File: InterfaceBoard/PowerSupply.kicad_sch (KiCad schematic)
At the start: 15 parts, among them U5 AP62250Z6

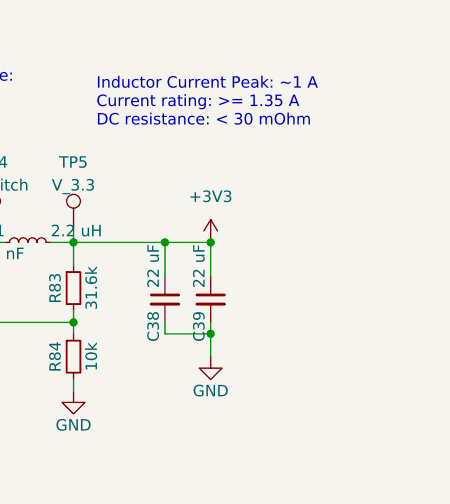
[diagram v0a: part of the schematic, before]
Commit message: InterfaceBoard: Routed some digital interfaces to MCU
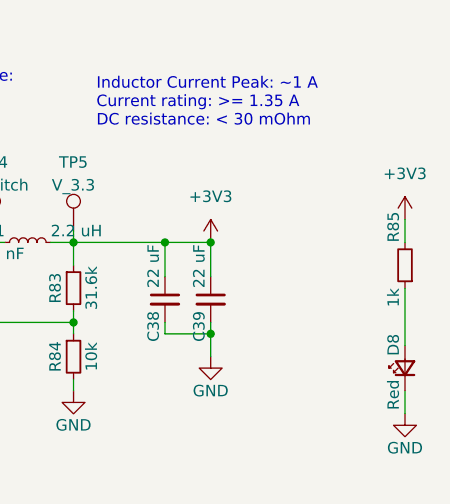
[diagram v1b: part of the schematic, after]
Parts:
- added D8: Red, LED_SMD:LED_0603_1608Metric, symbol Device:LED_Small
- added R85: 1k, Resistor_SMD:R_0603_1608Metric, symbol Device:R_Small
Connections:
- net +3V3: now also R85.2
- net GND: now also D8.1 (K)
- new net: D8.2 (A), R85.1
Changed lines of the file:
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@@
+    (stroke (width 0) (type default) (color 0 0 0 0))
+  )
+  (wire (pts (xy 213.36 87.63) (xy 213.36 90.17))
     (stroke (width 0) (type default) (color 0 0 0 0))
   )
@@
     (stroke (width 0) (type default) (color 0 0 0 0))
   )
+  (wire (pts (xy 213.36 106.68) (xy 213.36 109.22))
+    (stroke (width 0) (type default) (color 0 0 0 0))
+  )
   (wire (pts (xy 166.37 95.25) (xy 166.37 99.06))
     (stroke (width 0) (type default) (color 0 0 0 0))
@@
   )
   (wire (pts (xy 129.54 101.6) (xy 129.54 100.33))
+    (stroke (width 0) (type default) (color 0 0 0 0))
+  )
+  (wire (pts (xy 213.36 95.25) (xy 213.36 101.6))
     (stroke (width 0) (type default) (color 0 0 0 0))
   )
@@
     (effects (font (size 1.27 1.27)) (justify right))
   )
+  (symbol (lib_id "Device:R_Small") (at 213.36 92.71 180) (unit 1)
+    (in_bom yes) (on_board yes)
+    (property "Reference" "R85" (id 0) (at 212.09 90.17 90)
+      (effects (font (size 1.27 1.27)) (justify right))
+    )
+    (property "Value" "1k" (id 1) (at 212.09 95.25 90)
+      (effects (font (size 1.27 1.27)) (justify left))
+    )
+    (property "Footprint" "Resistor_SMD:R_0603_1608Metric" (id 2) (at 213.36 92.71 0)
+      (effects (font (size 1.27 1.27)) hide)
+    )
+    (property "Datasheet" "~" (id 3) (at 213.36 92.71 0)
+      (effects (font (size 1.27 1.27)) hide)
+    )
+    (pin "1")
+    (pin "2")
+  )
   (symbol (lib_id "power:GND") (at 176.53 106.68 0) (unit 1)
     (in_bom yes) (on_board yes)
@@
     )
     (pin "1")
+  )
+  (symbol (lib_id "Device:LED_Small") (at 213.36 104.14 90) (unit 1)
+    (in_bom yes) (on_board yes)
+    (property "Reference" "D8" (id 0) (at 212.09 100.33 0)
+      (effects (font (size 1.27 1.27)) (justify right))
+    )
+    (property "Value" "Red" (id 1) (at 212.09 105.41 0)
+      (effects (font (size 1.27 1.27)) (justify right))
+    )
+    (property "Footprint" "LED_SMD:LED_0603_1608Metric" (id 2) (at 213.36 104.14 90)
+      (effects (font (size 1.27 1.27)) hide)
+    )
+    (property "Datasheet" "~" (id 3) (at 213.36 104.14 90)
+      (effects (font (size 1.27 1.27)) hide)
+    )
+    (pin "1")
+    (pin "2")
   )
   (symbol (lib_id "power:GND") (at 148.59 101.6 0) (unit 1)
@@
     (pin "1")
   )
+  (symbol (lib_id "power:GND") (at 213.36 109.22 0) (unit 1)
+    (in_bom yes) (on_board yes)
+    (property "Reference" "#PWR0186" (id 0) (at 213.36 115.57 0)
+      (effects (font (size 1.27 1.27)) hide)
+    )
+    (property "Value" "GND" (id 1) (at 213.36 113.03 0))
+    (property "Footprint" "" (id 2) (at 213.36 109.22 0)
+      (effects (font (size 1.27 1.27)) hide)
+    )
+    (property "Datasheet" "" (id 3) (at 213.36 109.22 0)
+      (effects (font (size 1.27 1.27)) hide)
+    )
+    (pin "1")
+  )
   (symbol (lib_id "power:+3V3") (at 191.77 90.17 0) (unit 1)
     (in_bom yes) (on_board yes) (fields_autoplaced)
@@
     (pin "2")
   )
+  (symbol (lib_id "power:+3V3") (at 213.36 87.63 0) (unit 1)
+    (in_bom yes) (on_board yes) (fields_autoplaced)
+    (property "Reference" "#PWR0185" (id 0) (at 213.36 91.44 0)
+      (effects (font (size 1.27 1.27)) hide)
+    )
+    (property "Value" "+3V3" (id 1) (at 213.36 82.55 0))
+    (property "Footprint" "" (id 2) (at 213.36 87.63 0)
+      (effects (font (size 1.27 1.27)) hide)
+    )
+    (property "Datasheet" "" (id 3) (at 213.36 87.63 0)
+      (effects (font (size 1.27 1.27)) hide)
+    )
+    (pin "1")
+  )
   (symbol (lib_id "Device:C_Small") (at 163.83 92.71 90) (unit 1)

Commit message: InterfaceBoard: Rev 1.0
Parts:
- removed R80, R81, R82: 0, Resistor_SMD:R_0603_1608Metric, symbol Device:R_Small
- added J5: Conn_02x03_Odd_Even, Connector_PinHeader_1.27mm:PinHeader_2x03_P1.27mm_Vertical, symbol Connector_Generic:Conn_02x03_Odd_Even
- TP4: renamed from TP5; value V_3.3 -> 3V3
- renumbered C37 to C12, C35 to C13, C36 to C14, C39 to C15, C38 to C16, D8 to D3, R85 to R24, R84 to R29, R83 to R32, TP4 to TP7, U5 to U3
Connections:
- net +15V: now also J5.3 (Pin_3)
- net V_EXT: now also J5.5 (Pin_5)
- net V_IN: now also J5.2 (Pin_2), J5.4 (Pin_4), J5.6 (Pin_6)
- net V_USB: now also J5.1 (Pin_1)
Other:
- note removed: "Only populate one Or use diodes"
- company: (none) -> Peter Farley
- title: (none) -> Kiethley 615 Interface Board

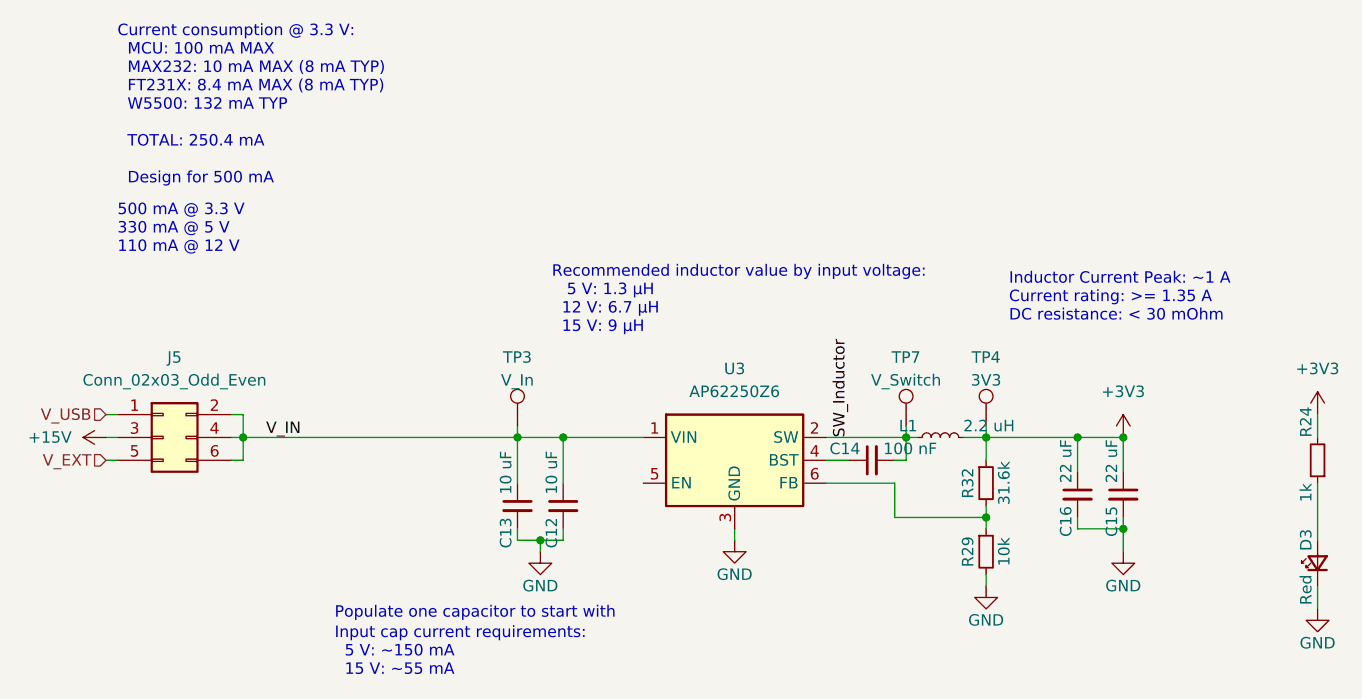
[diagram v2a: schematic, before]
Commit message: InterfaceBoard: Add BOM
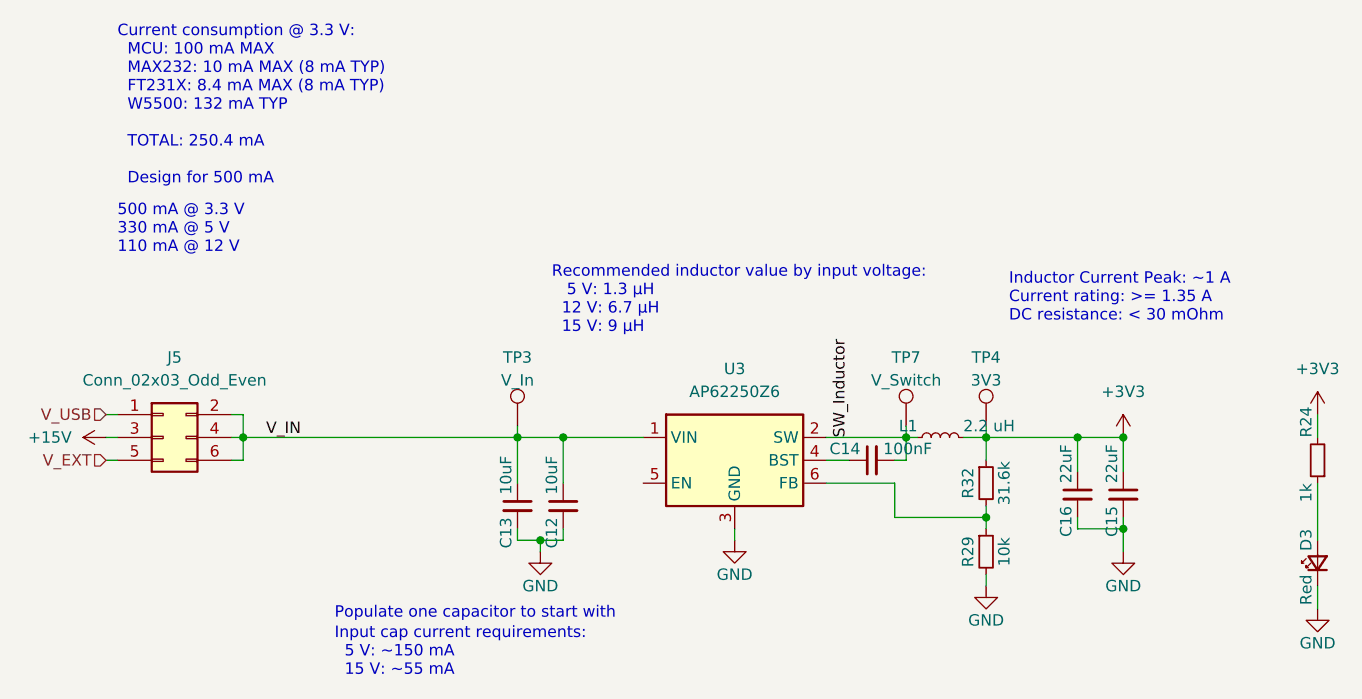
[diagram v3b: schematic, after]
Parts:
- C12, C13: value 10 uF -> 10uF
- C14: value 100 nF -> 100nF; DigiKey (none) -> https://www.digikey.com/en/products/detail/samsung-electro-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
- C15, C16: value 22 uF -> 22uF
- D3: DigiKey (none) -> https://www.digikey.com/en/products/detail/harvatek-corpora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
- R24: DigiKey (none) -> https://www.digikey.com/en/products/detail/walsin-technolog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
- R29: DigiKey (none) -> https://www.digikey.com/en/products/detail/yageo/RC0603FR-1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
- R32: DigiKey (none) -> https://www.digikey.com/en/products/detail/bourns-inc/CR060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
- U3: DigiKey (none) -> https://www.digikey.com/en/products/detail/diodes-incorpora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
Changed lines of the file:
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@@
+      (effects (font (size 1.27 1.27)) hide)
+    )
+    (property "DigiKey" "https://www.digikey.com/en/products/detail/walsin-technology-corporation/WR06X102-JTL/13241138" (id 4) (at 213.36 92.71 0)
       (effects (font (size 1.27 1.27)) hide)
     )
@@
       (effects (font (size 1.27 1.27)) hide)
     )
+    (property "DigiKey" "https://www.digikey.com/en/products/detail/harvatek-corporation/B1911USD-20D000114U1930/15519991" (id 4) (at 213.36 104.14 0)
+      (effects (font (size 1.27 1.27)) hide)
+    )
     (pin "1")
     (pin "2")
@@
     )
     (property "Datasheet" "~" (id 3) (at 176.53 95.25 0)
+      (effects (font (size 1.27 1.27)) hide)
+    )
+    (property "DigiKey" "https://www.digikey.com/en/products/detail/bourns-inc/CR0603-FX-3162ELF/3783940" (id 4) (at 176.53 95.25 0)
       (effects (font (size 1.27 1.27)) hide)
     )
@@
       (effects (font (size 1.27 1.27)) (justify right))
     )
-    (property "Value" "22 uF" (id 1) (at 185.42 95.25 90)
+    (property "Value" "22uF" (id 1) (at 185.42 95.25 90)
       (effects (font (size 1.27 1.27)) (justify left))
     )
@@
       (effects (font (size 1.27 1.27)) (justify right))
     )
-    (property "Value" "10 uF" (id 1) (at 128.27 96.52 90)
+    (property "Value" "10uF" (id 1) (at 128.27 96.52 90)
       (effects (font (size 1.27 1.27)) (justify left))
     )
@@
       (effects (font (size 1.27 1.27)) (justify right))
     )
-    (property "Value" "22 uF" (id 1) (at 190.5 95.25 90)
+    (property "Value" "22uF" (id 1) (at 190.5 95.25 90)
       (effects (font (size 1.27 1.27)) (justify left))
     )
@@
       (effects (font (size 1.27 1.27)) (justify right))
     )
-    (property "Value" "10 uF" (id 1) (at 123.19 96.52 90)
+    (property "Value" "10uF" (id 1) (at 123.19 96.52 90)
       (effects (font (size 1.27 1.27)) (justify left))
     )
@@
     )
     (property "Datasheet" "~" (id 3) (at 176.53 102.87 0)
+      (effects (font (size 1.27 1.27)) hide)
+    )
+    (property "DigiKey" "https://www.digikey.com/en/products/detail/yageo/RC0603FR-1010KL/12756395" (id 4) (at 176.53 102.87 0)
       (effects (font (size 1.27 1.27)) hide)
     )
@@
       (effects (font (size 1.27 1.27)) hide)
     )
+    (property "DigiKey" "https://www.digikey.com/en/products/detail/diodes-incorporated/AP62250Z6-7/12349310" (id 4) (at 148.59 92.71 0)
+      (effects (font (size 1.27 1.27)) hide)
+    )
     (pin "1")
     (pin "2")
@@
       (effects (font (size 1.27 1.27)) (justify left))
     )
-    (property "Value" "100 nF" (id 1) (at 165.1 91.44 90)
+    (property "Value" "100nF" (id 1) (at 165.1 91.44 90)
       (effects (font (size 1.27 1.27)) (justify right))
     )
@@
       (effects (font (size 1.27 1.27)) hide)
     )
+    (property "DigiKey" "https://www.digikey.com/en/products/detail/samsung-electro-mechanics/CL10B104KB8NNWC/3887593" (id 4) (at 163.83 92.71 0)
+      (effects (font (size 1.27 1.27)) hide)
+    )
